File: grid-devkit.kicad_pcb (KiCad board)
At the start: 4 copper layers, 29.1 x 100.3 mm, 168 parts, among them J601 TYPE-C-32-M-12, J603 Conn_01x04, J604 Conn_01x04, J610 Conn_01x08, J611 Conn_01x08, J701 C5137195, J702 Conn_02x05_Odd_Even, SW609 model_code, SW610 rev_code, SW701 C255807, SW702 C2905169, SW703 C2905169, U1001 74HC4051, U1002 74HC4051, U601 LN1134A332MR-G, U602 C5451661, U603 C5451661, U604 74LVC1G08, U605 BL1551B, U606 BL1551B, U607 BL1551B, U608 BL1551B, U609 74HC165, U610 APS1604M-3SQR-ZR, U703 RP2040, U704 ESP32-S3, U705 W25Q64JVSSIQ, U801 74HC165, U903 APS1604M-3SQR-SN, U918 NS4168_C910588, Y701 40MHz

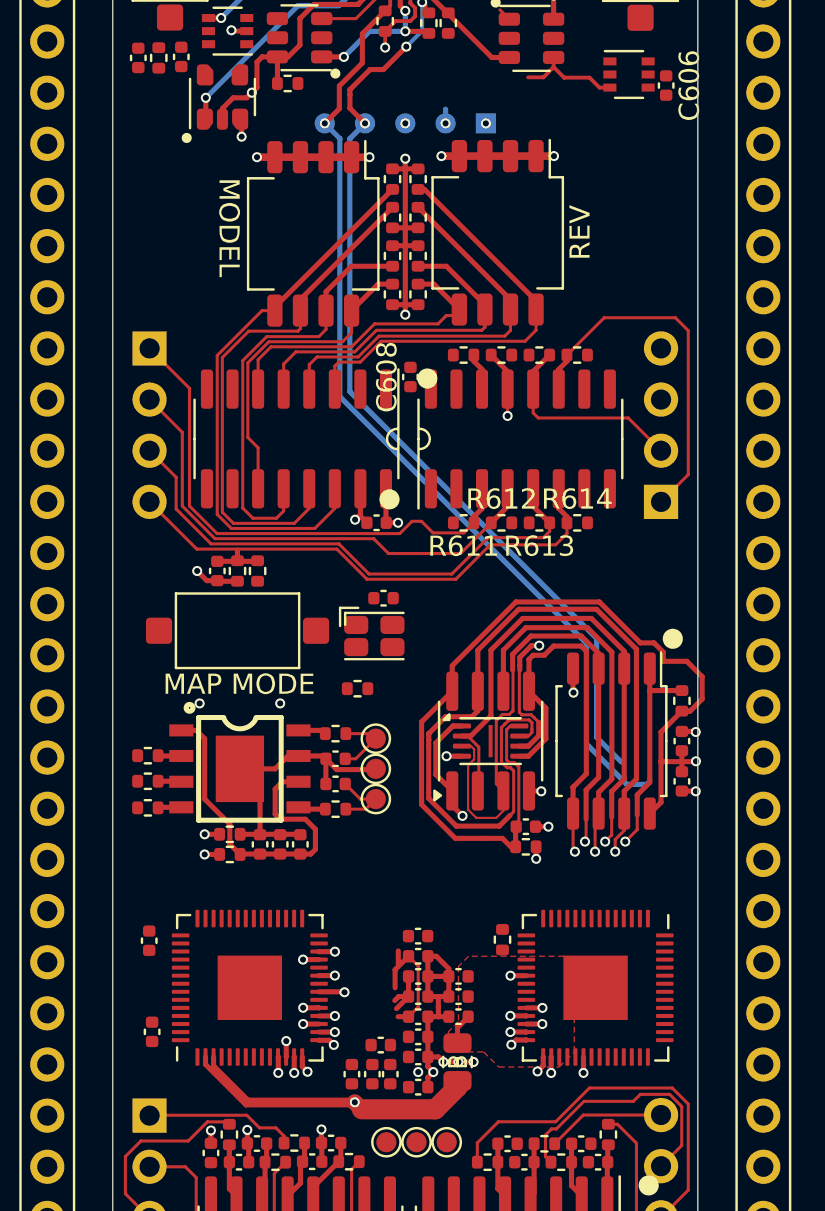
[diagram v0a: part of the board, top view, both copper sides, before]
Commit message: Adds traces
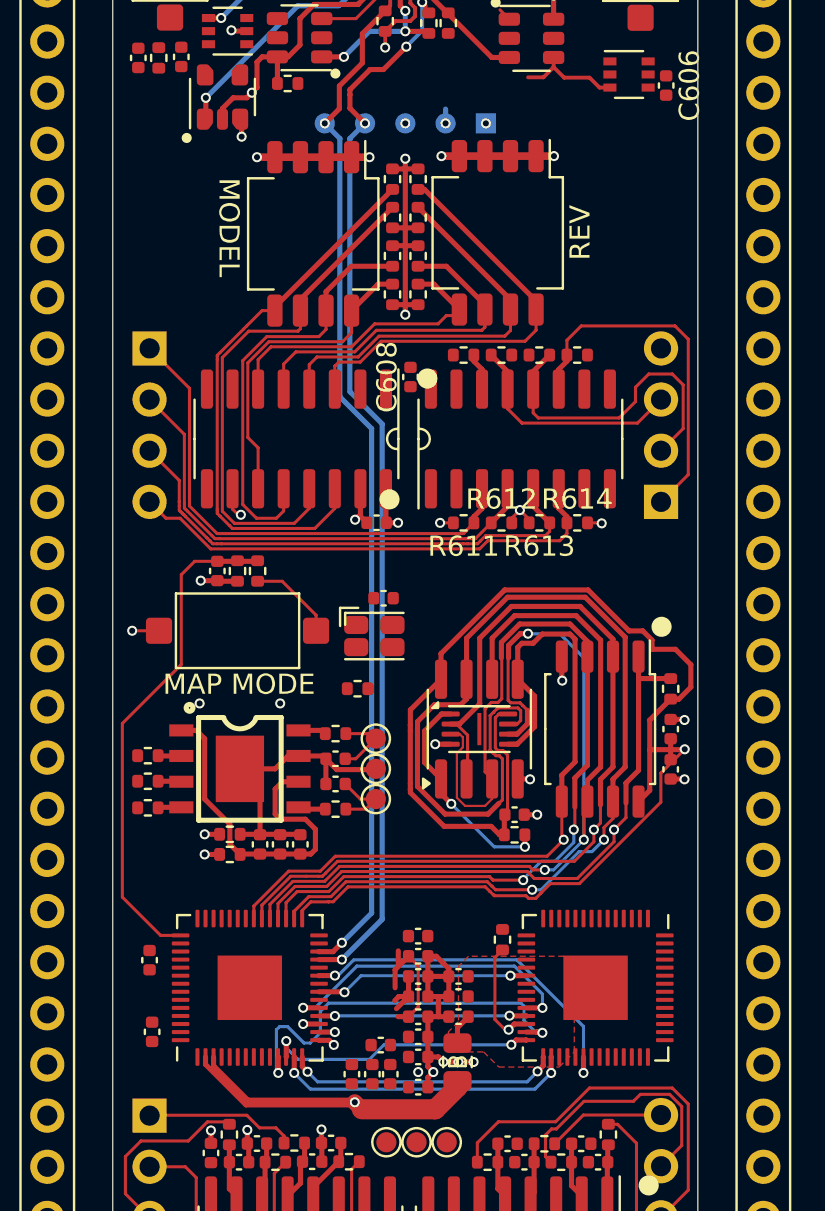
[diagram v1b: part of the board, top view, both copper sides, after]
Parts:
- moved C751 0.97 mm to (87.3, 105.0)
- moved C755 0.82 mm to (113.2, 93.5)
- moved C921 0.82 mm to (105.4, 97.8)
- moved R734 0.82 mm to (113.2, 91.5)
- moved U610 0.82 mm to (103.7, 93.5)
- moved U705 0.82 mm to (109.7, 93.5)
- moved U903 0.82 mm to (103.7, 93.5)
- moved C756 0.82 mm to (113.2, 95.5)
- moved R904 0.82 mm to (105.4, 98.8)
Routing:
- net /MCU/SPICLK: track 25.8 -> 55.9 mm, vias 2 -> 3
- net VDD_SPI: track 46.5 -> 70.5 mm
- net /MCU/MAP_MODE: track 2.50 -> 24.9 mm
- net /MCU/SPICS0: track 10.7 -> 30.3 mm
- net /MCU/SPIQ: track 26.2 -> 45.2 mm
- net /MCU/RP_SPI0_RX: track 1.59 -> 19.9 mm
- net /MCU/SPIHD: track 41.7 -> 59.3 mm, vias 1 -> 2
- net /MCU/SPID: track 19.5 -> 36.8 mm
- net /MCU/SPIWP: track 28.9 -> 46.0 mm, vias 1 -> 2
- net /MCU/RP_INTERRUPT: track 1.58 -> 17.9 mm
- net /MCU/RP_SWCLK: track 1.59 -> 15.6 mm
- net /MCU/RP_SPI0_TX: track 1.59 -> 15.0 mm
- net /MCU/RP_SPI0_CS: track 1.63 -> 13.7 mm
- net /MCU/RP_SPI0_SCK: track 1.68 -> 13.5 mm
- net /MCU/RP_SWDIO: track 1.59 -> 10.3 mm
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
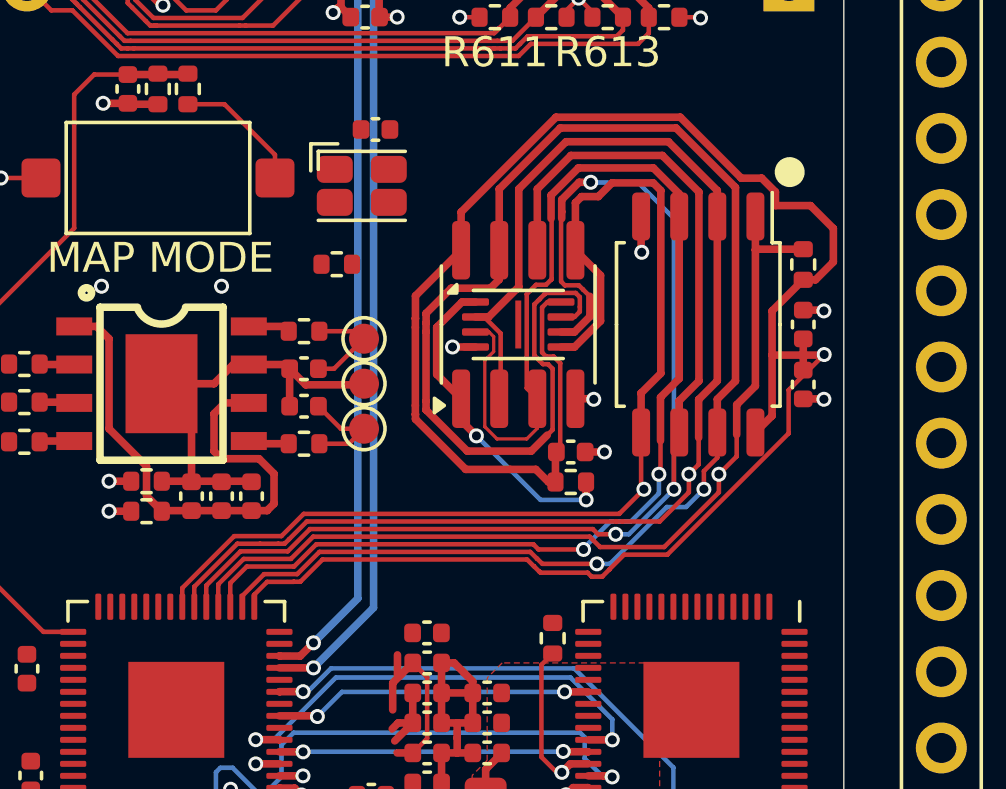
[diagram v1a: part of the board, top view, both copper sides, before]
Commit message: Adds traces
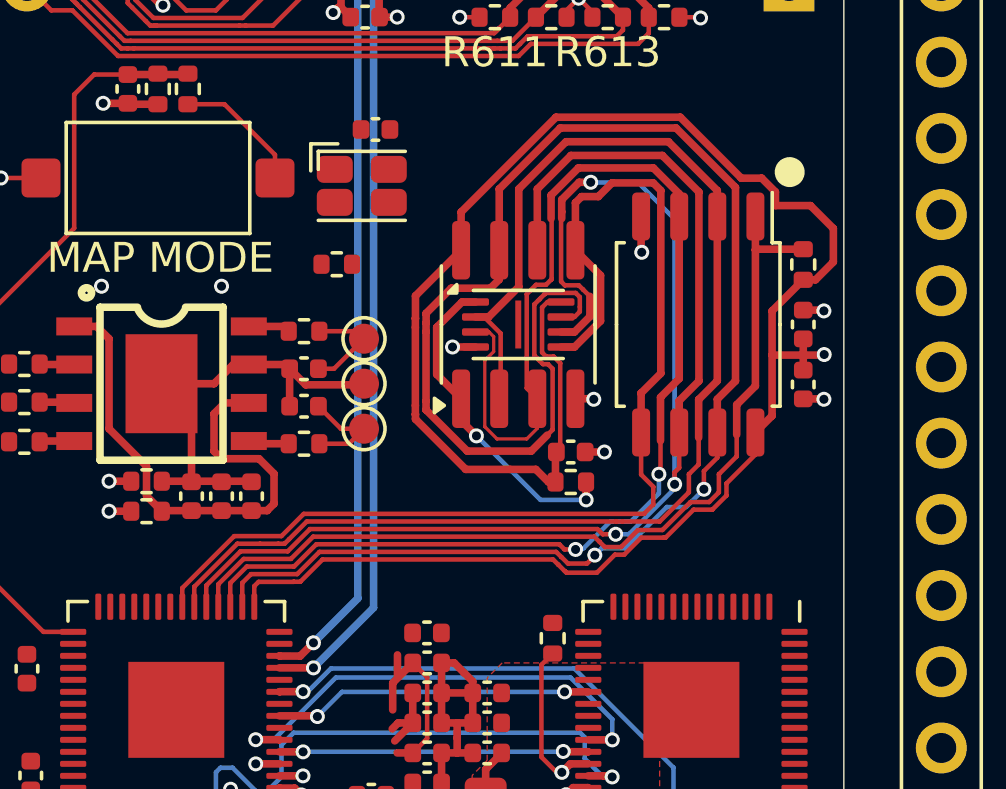
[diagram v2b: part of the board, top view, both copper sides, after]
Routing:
- net VDD_SPI: track 70.5 -> 67.0 mm
- net /MCU/SPID: track 36.8 -> 37.6 mm, vias 1 -> 0
- net /MCU/SPIQ: vias 1 -> 0
- net /MCU/SPICS0: vias 1 -> 0

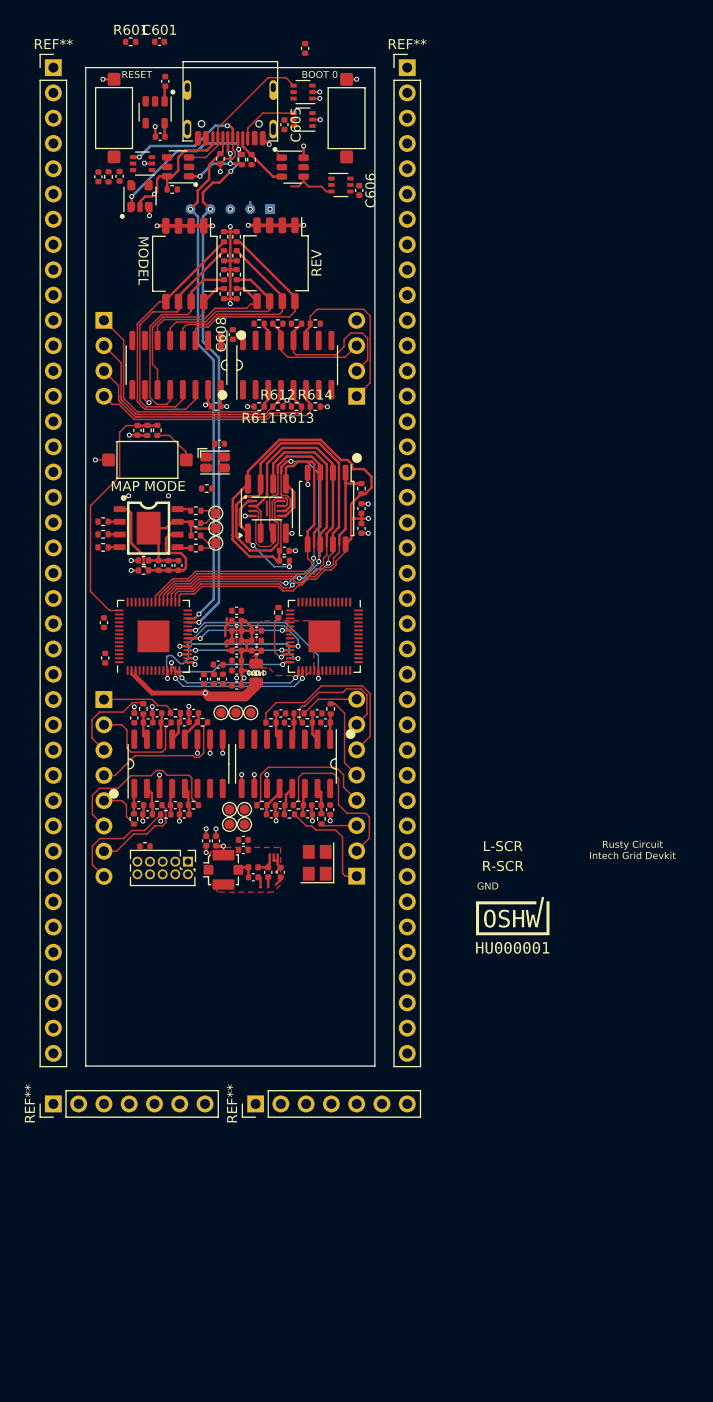
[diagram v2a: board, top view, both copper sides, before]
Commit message: SUKU antenna and xtal layout done
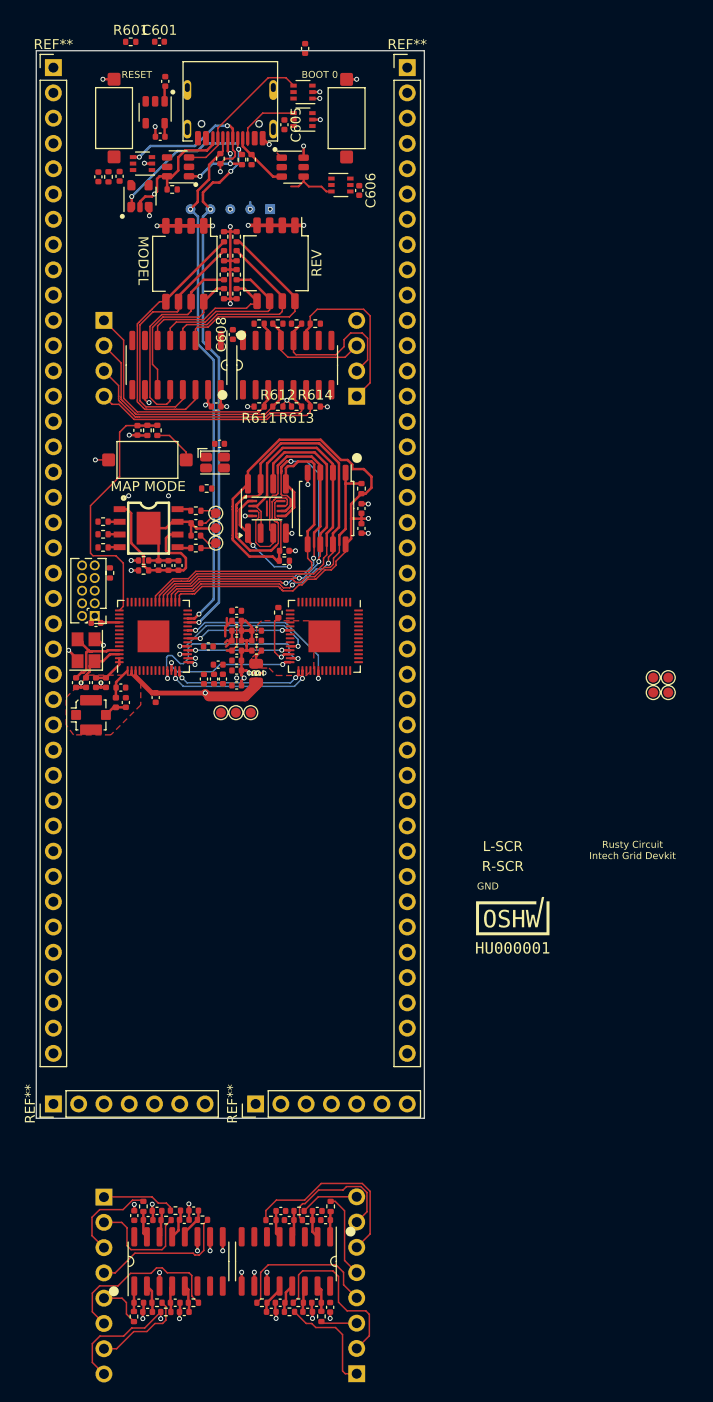
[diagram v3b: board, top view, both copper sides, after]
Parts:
- moved C1002 50.0 mm to (91.7, 165.0)
- moved C1009 50.0 mm to (90.3, 164.6)
- moved C1010 50.0 mm to (105.0, 173.3)
- moved C1011 50.0 mm to (108.7, 173.3)
- moved C1018 50.0 mm to (110.0, 173.8)
- moved R1005 50.0 mm to (93.5, 165.0)
- moved R1013 50.0 mm to (106.8, 173.3)
- moved R1014 50.0 mm to (103.2, 173.3)
- moved C1003 50.0 mm to (90.8, 173.3)
- moved C1004 50.0 mm to (91.7, 174.2)
- moved C1006 50.0 mm to (96.3, 164.1)
- moved C1007 50.0 mm to (95.4, 174.2)
- moved C1008 50.0 mm to (94.5, 173.3)
- moved C1012 50.0 mm to (109.6, 165.0)
- moved C1016 50.0 mm to (105.1, 164.1)
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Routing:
- net Net-(U704-XTAL_N): track 0.69 -> 8.10 mm, vias 1 -> 0
- net +3V3: track 25.2 -> 30.6 mm
- net Net-(U704-XTAL_P): track 0.80 -> 4.80 mm, vias 1 -> 0
- net Net-(C749-Pad1): track 26.0 -> 22.9 mm
- net /MCU/ESP_LNA: track 1.98 -> 3.22 mm
- net /MCU/MAP_MODE: track 24.9 -> 26.0 mm
- net Net-(J701-In): track 1.76 -> 2.31 mm
- net GND: track 60.1 -> 60.3 mm, vias 36 -> 38
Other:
- board size 29.1 x 100.3 mm -> 39 x 107.3 mm

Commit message: SUKU mcu positioning and grids fixed, decoupling capacitors placed and routed
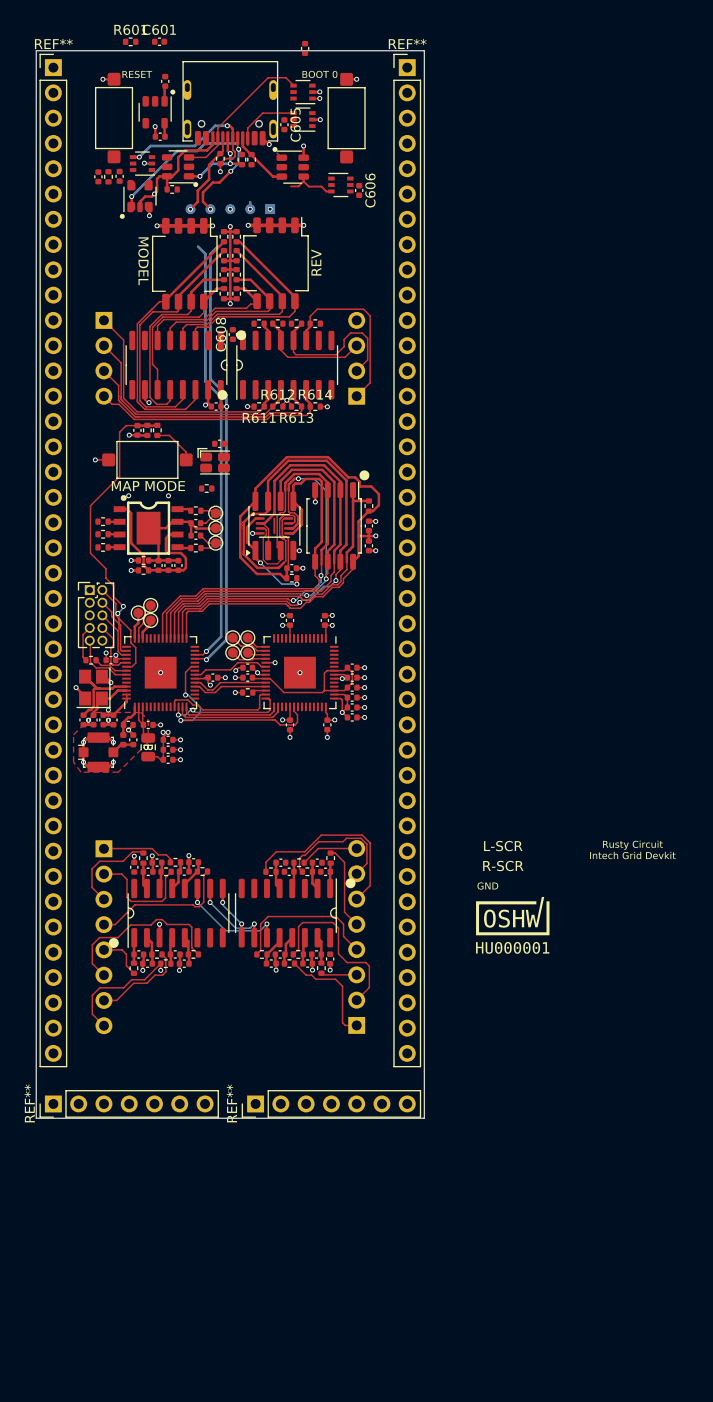
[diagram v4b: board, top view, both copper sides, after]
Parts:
- moved TP702 42.4 mm to (100.2, 106.5)
- moved TP704 42.4 mm to (100.2, 108.0)
- moved TP701 42.4 mm to (101.8, 106.5)
- moved TP703 42.4 mm to (101.8, 108.0)
- moved C1001 35.0 mm to (95.4, 130.0)
- moved C1002 35.0 mm to (91.7, 130.0)
- moved C1003 35.0 mm to (90.8, 138.3)
- moved C1004 35.0 mm to (91.7, 139.2)
- moved C1005 35.0 mm to (92.6, 129.1)
- moved C1006 35.0 mm to (96.3, 129.1)
- moved C1007 35.0 mm to (95.4, 139.2)
- moved C1008 35.0 mm to (94.5, 138.3)
- moved C1009 35.0 mm to (90.3, 129.6)
- moved C1010 35.0 mm to (105.0, 138.3)
- moved C1011 35.0 mm to (108.7, 138.3)
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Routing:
- net +3V3: track 30.6 -> 54.6 mm, vias 11 -> 24
- net Net-(C749-Pad1): track 22.9 -> 5.39 mm, vias 1 -> 0
- net +1V1: track 6.43 -> 17.0 mm
- net GND: track 60.3 -> 70.6 mm, vias 38 -> 59
- net ESP_GPIO_42: track 0.00 -> 9.81 mm
- net /MCU/RP_SPI0_RX: track 19.9 -> 11.6 mm, vias 2 -> 0
- net /MCU/RP_SWCLK: track 15.6 -> 7.74 mm, vias 2 -> 0
- net ESP_GPIO_44: track 0.00 -> 6.33 mm
- net ESP_GPIO_39: track 0.00 -> 6.13 mm
- net ESP_GPIO_41: track 0.00 -> 5.83 mm
- net ESP_GPIO_40: track 0.00 -> 5.26 mm
- net /MCU/RP_INTERRUPT: track 17.9 -> 22.0 mm
- net /MCU/RP_RUN: track 5.50 -> 1.39 mm, vias 1 -> 0
- net Net-(U703-GPIO13): track 0.00 -> 3.85 mm
- net ESP_GPIO_36: track 0.00 -> 3.81 mm
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- added copper zone on In2.Cu, net +3V3
- added copper zone on In1.Cu, net GND
- removed copper zone on F.Cu, net +3V3
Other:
- board text added: "ESP32 POSITION (x = 93, y = 110) RP2040 POSITION (x = 107, y = 110) GRID = 0.25mm"
